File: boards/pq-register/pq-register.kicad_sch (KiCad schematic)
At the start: 48 parts, among them P1 Card Edge, Q51 MMBT5401, Q52 MMBT5401, Q53 MMBT5401, Q54 MMBT5401, Q55 MMBT5401, Q56 MMBT5401, Q97 MMBT5401, Q98 MMBT5401, Q99 MMBT5401

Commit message: Route resistors in the second column.
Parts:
- R267, R496: value 2k ½W -> 800R 2W; footprint Resistor_SMD:R_1210_3225Metric -> Resistor_THT:R_Axial_DIN0516_L15.5mm_D5.0mm_P20.32mm_Horizontal
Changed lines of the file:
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@@
 			)
 		)
-		(property "Value" "2k ½W"
+		(property "Value" "800R 2W"
 			(at 180.594 66.04 0)
 			(show_name no)
@@
 			)
 		)
-		(property "Footprint" "Resistor_SMD:R_1210_3225Metric"
+		(property "Footprint" "Resistor_THT:R_Axial_DIN0516_L15.5mm_D5.0mm_P20.32mm_Horizontal"
 			(at 178.054 65.024 90)
 			(hide yes)
@@
 			)
 		)
-		(property "Value" "2k ½W"
+		(property "Value" "800R 2W"
 			(at 180.594 107.95 0)
 			(show_name no)
@@
 			)
 		)
-		(property "Footprint" "Resistor_SMD:R_1210_3225Metric"
+		(property "Footprint" "Resistor_THT:R_Axial_DIN0516_L15.5mm_D5.0mm_P20.32mm_Horizontal"
 			(at 178.054 106.934 90)
 			(hide yes)
@@
 		)
 	)
-	(group ""
-		(lib_id "Project:nor")
-		(members "42d083b2-6620-49b4-9538-79b166fe935b" "48528367-d2e7-44a7-bc4a-72f7fcc8578e"
-			"79f5f5d1-dc11-47ac-a7fb-02cd3902d52f" "9aeb7502-e8a6-4085-9942-11c499e606e6"
-			"d2bcef0a-675e-4bbe-a479-ad5b87f55745" "d3423006-9dd8-46b0-97fa-726bde51498d"
-			"eda4eb1e-5498-472b-ad48-dab45ecac28b" "ee2e61a6-7370-4f1d-93b9-24064a518ef6"
-			"eea3afc0-4e78-4469-b389-770e1c660dc0" "f40bb5e1-9fcd-4a22-9ca3-c136e4fd30ee"
-			"f700d24b-2379-441a-97b5-bccc91968f9f" "fce78a0b-1a40-4317-9603-059b53e14ceb"
-		)
-	)

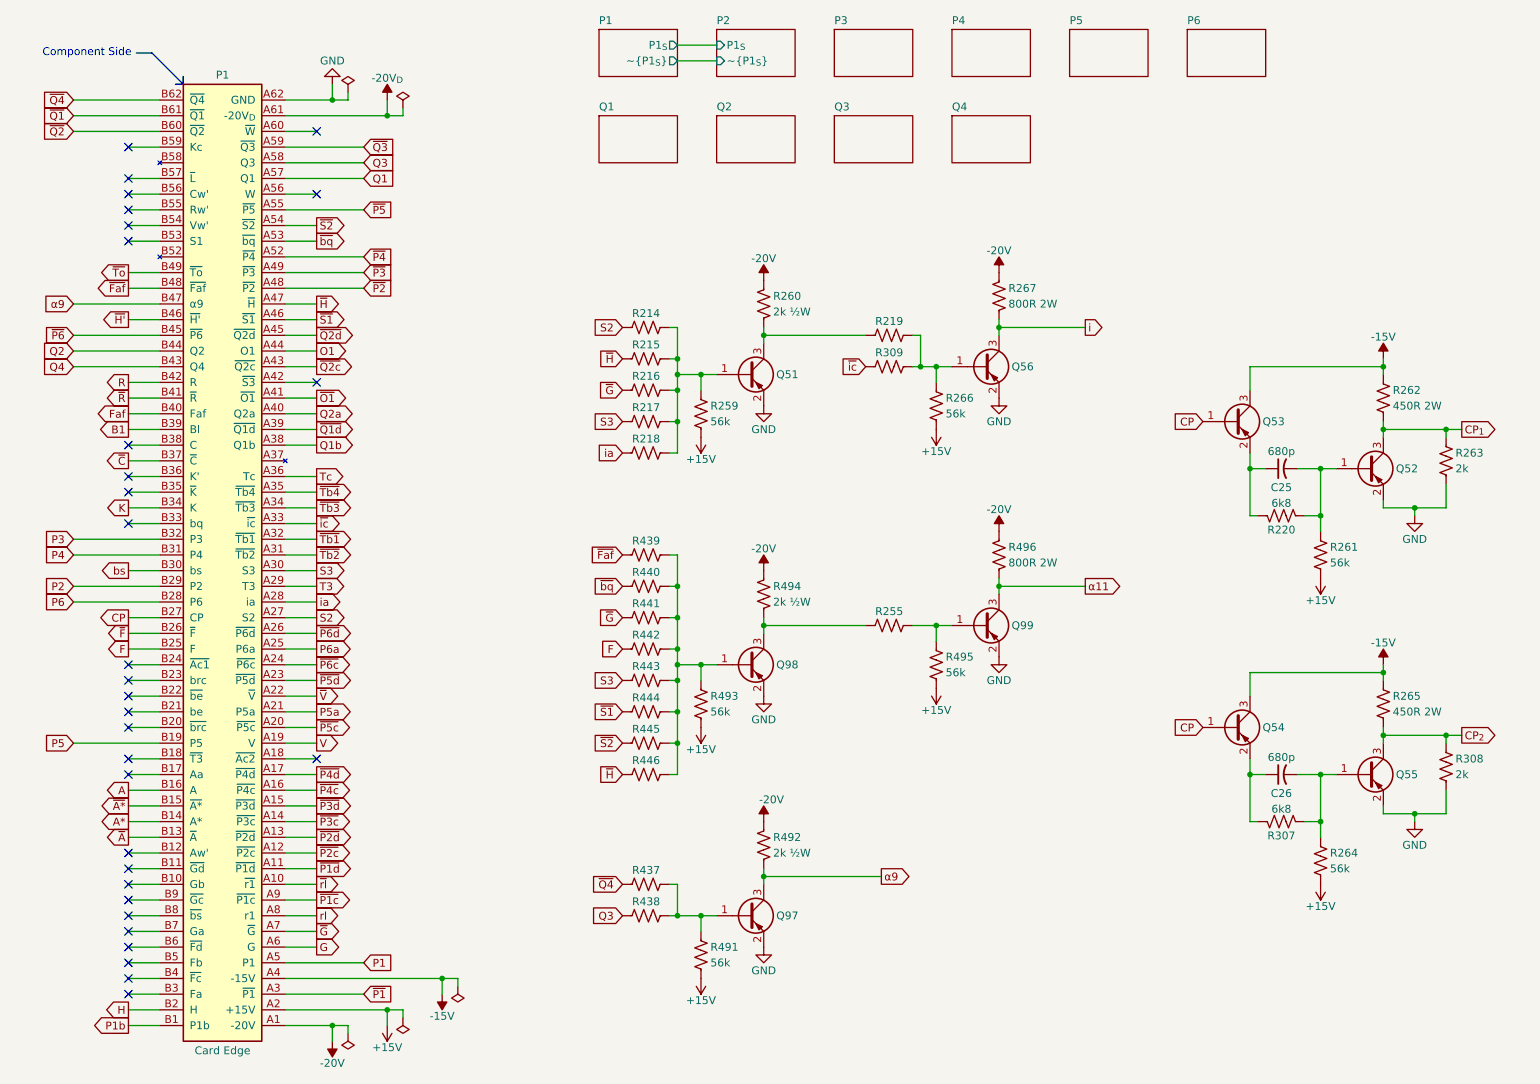
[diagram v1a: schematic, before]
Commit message: Route all remaining passives.
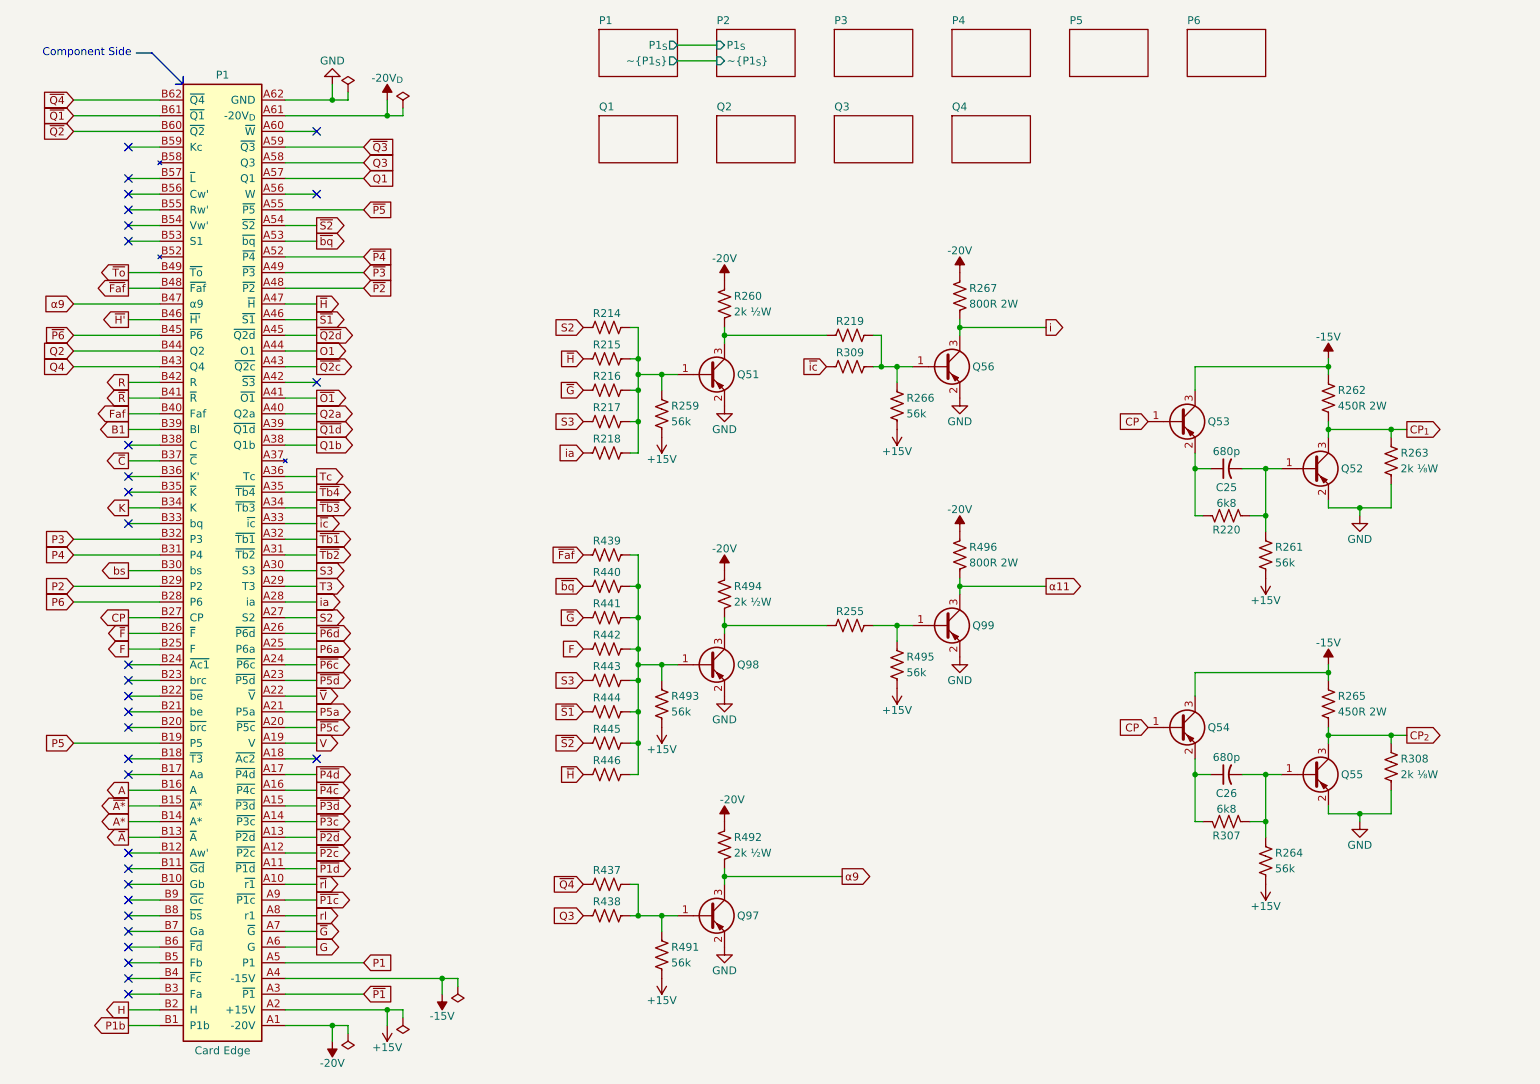
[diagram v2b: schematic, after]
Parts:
- R263, R308: value 2k -> 2k ⅛W; footprint Resistor_SMD:R_1206_3216Metric -> Resistor_SMD:R_0805_2012Metric
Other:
- moved on the sheet: C25, C26, Q51, Q52, Q53, Q54, Q55, Q56, Q97, Q98, Q99, R214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

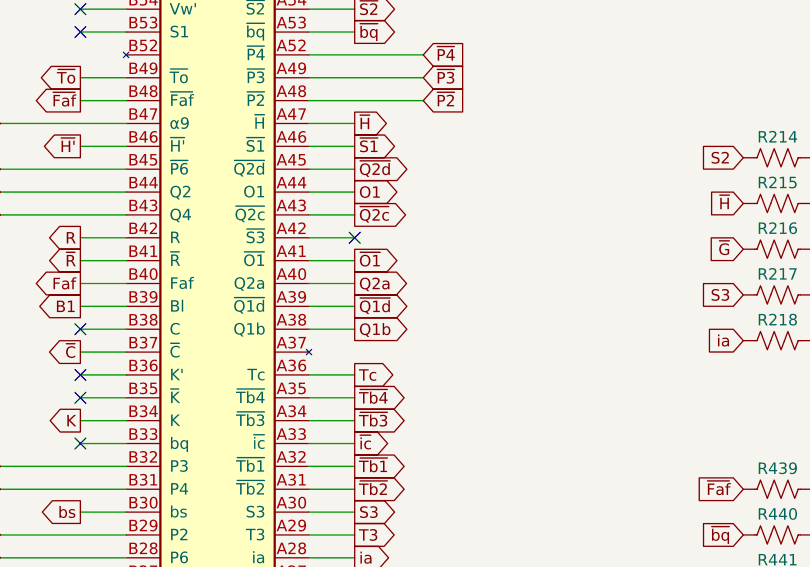
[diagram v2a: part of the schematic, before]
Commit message: Rough route the left column.
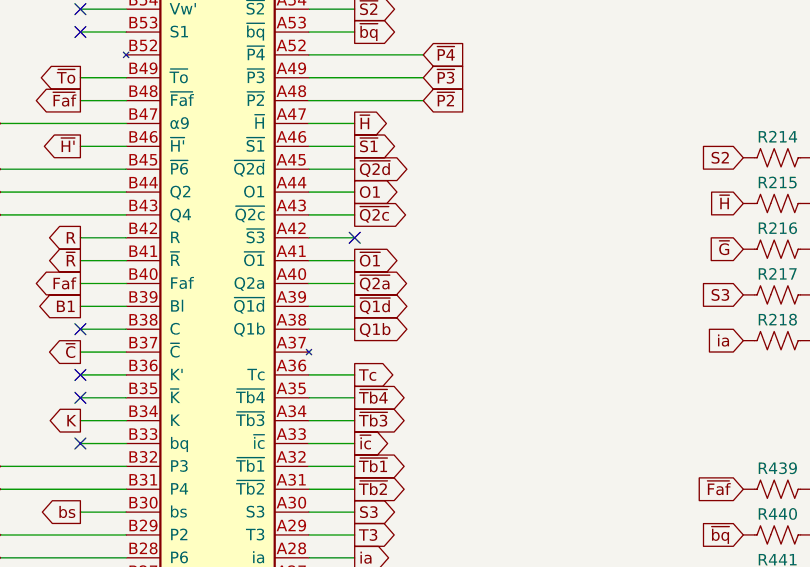
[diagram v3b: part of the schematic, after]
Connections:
- net Q2a renamed ~{Q2a}
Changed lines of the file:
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@@
 		)
 	)
-	(global_label "Q2a"
+	(global_label "~{Q2a}"
 		(shape output)
 		(at 68.58 83.82 0)

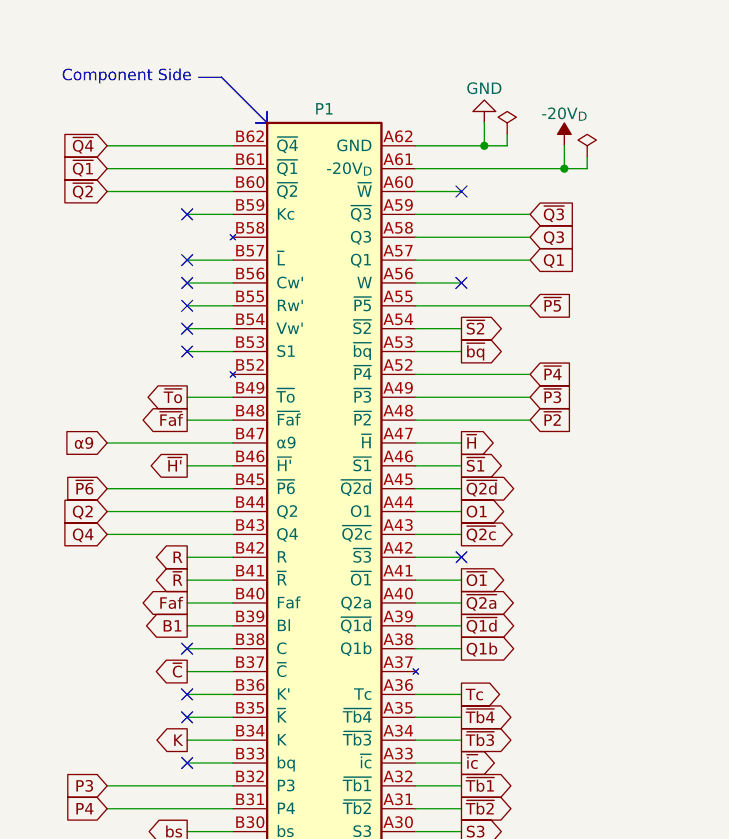
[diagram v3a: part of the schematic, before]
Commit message: Add tooling holes and clean up for template.
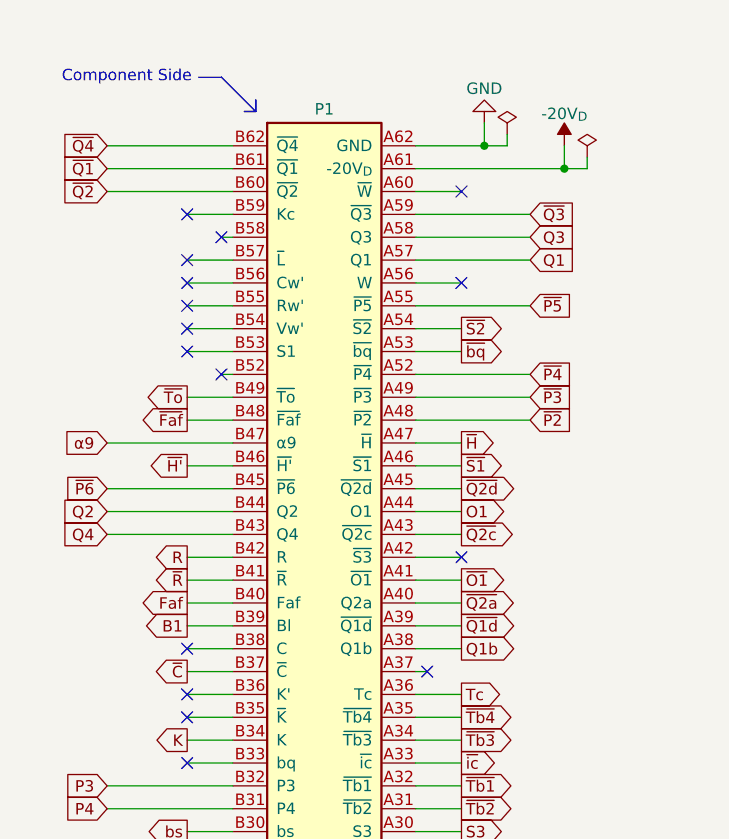
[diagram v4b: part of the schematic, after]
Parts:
- P1: footprint Project:Bus_PCI_5V_32bit -> 0Project:Bus_PCI_5V_32bit; symbol Project:Backplane -> 0Project:Backplane
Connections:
- no-connect marks 31 -> 34
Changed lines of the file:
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@@
 	)
 	(rectangle
-		(start 46.99 29.21)
-		(end 46.99 30.48)
+		(start 45.72 27.94)
+		(end 45.72 29.21)
 		(stroke
 			(width 0)
@@
 	)
 	(rectangle
-		(start 45.72 30.48)
-		(end 46.99 30.48)
+		(start 44.45 29.21)
+		(end 45.72 29.21)
 		(stroke
 			(width 0)
@@
 	)
 	(no_connect
+		(at 64.77 91.44)
+	)
+	(no_connect
 		(at 68.58 78.74)
 	)
@@
 	)
 	(no_connect
+		(at 41.91 58.42)
+	)
+	(no_connect
 		(at 38.1 124.46)
 	)
@@
 	)
 	(no_connect
+		(at 41.91 43.18)
+	)
+	(no_connect
 		(at 68.58 139.7)
 	)
@@
 	(wire
 		(pts
+			(xy 41.91 58.42) (xy 43.18 58.42)
+		)
+		(stroke
+			(width 0)
+			(type default)
+		)
+	)
+	(wire
+		(pts
 			(xy 63.5 35.56) (xy 80.01 35.56)
 		)
@@
 	(wire
 		(pts
+			(xy 63.5 91.44) (xy 64.77 91.44)
+		)
+		(stroke
+			(width 0)
+			(type default)
+		)
+	)
+	(wire
+		(pts
 			(xy 63.5 111.76) (xy 68.58 111.76)
 		)
@@
 	(polyline
 		(pts
-			(xy 41.91 25.4) (xy 46.99 30.48)
+			(xy 41.91 25.4) (xy 45.72 29.21)
 		)
 		(stroke
@@
 	(wire
 		(pts
+			(xy 41.91 43.18) (xy 43.18 43.18)
+		)
+		(stroke
+			(width 0)
+			(type default)
+		)
+	)
+	(wire
+		(pts
 			(xy 172.72 110.49) (xy 172.72 111.76)
 		)
@@
 	)
 	(symbol
-		(lib_id "Project:Backplane")
+		(lib_id "0Project:Backplane")
 		(at 53.34 106.68 0)
 		(unit 1)
@@
 			)
 		)
-		(property "Footprint" "Project:Bus_PCI_5V_32bit"
+		(property "Footprint" "0Project:Bus_PCI_5V_32bit"
 			(at 73.66 6.096 0)
 			(hide yes)

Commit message: Add script to export production files.
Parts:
- C25, C26: BOM Value (none) -> 680pF
- P1: now left out of the parts list
- Q51, Q52, Q53, Q54, Q55, Q56, Q97, Q98, Q99: BOM Value (none) -> MMBT5401; LCSC (none) -> C8326
- R214, R215, R216, R217, R218, R219, R255, R309, R437, R438, R439, R440, R441, R442, R443, R444, R445, R446: BOM Value (none) -> 15kΩ
- R220, R307: BOM Value (none) -> 6.8kΩ
- R259, R261, R264, R266, R491, R493, R495: BOM Value (none) -> 56kΩ
- R260, R492, R494: BOM Value (none) -> 2kΩ 500mW
- R262, R265: BOM Value (none) -> 450Ω 2W
- R263, R308: BOM Value (none) -> 2kΩ 125mW
- R267, R496: BOM Value (none) -> 800Ω 2W
